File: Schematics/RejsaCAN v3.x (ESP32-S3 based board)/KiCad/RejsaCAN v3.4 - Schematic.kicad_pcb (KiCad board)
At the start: 2 copper layers, 65 parts, among them Q1 SS8050, U1 ESP32-S3-WROOM-1(N16R8), U2 SN65HVD230DR, U3 ME2807A33M3G, U4 LMR14006XDDCR, U5 MT9700

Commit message: Add v3.4 board outline and mounting holes, traced from the fabricated Gerbers
The KiCad board had no Edge.Cuts geometry at all, which blocks placement,
routing and any real fab quote (board price is a function of dimensions).

Both the outline and the holes are derived from upstream manufacturing data
rather than drawn by eye:

  Gerber_BoardOutlineLayer.GKO  -> 8-corner Edge.Cuts profile
  Drill_NPTH_Through.DRL, T03   -> four 2.59mm NPTH mounting holes

Result is 31.496 x 49.530 mm with the 18.034 x 5.969 mm notch between the
top tabs. Verified by exporting Edge.Cuts back out through kicad-cli and
re-measuring: dimensions match the source Gerber, and the notch sits 6.731mm
from both side edges.

Two deliberate choices:

- EasyEDA exported the notch's left wall 0.0007in off vertical. Snapped to
  the mirrored value so both walls are truly vertical; 18um, below any fab
  tolerance, but it makes the outline exactly symmetric as intended.
- The holes are 2.59mm, matching the fabricated board. Stock KiCad offers
  2.5mm (tight for M2.5) and 2.7mm (loose), so RejsaCAN.pretty gains
  MountingHole_2.59mm_NPTH. They carry the board_only attribute, so Update
  PCB from Schematic will not delete them for having no symbol -- confirmed
  by DRC reporting zero schematic-parity errors.

Also gitignores generated fabrication output while keeping a README that
documents how to regenerate it.

Co-Authored-By: Claude Opus 5 (1M context) <noreply@anthropic.com>
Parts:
- added H1: MountingHole_2.59mm_NPTH, RejsaCAN:MountingHole_2.59mm_NPTH, F.Cu at (112.0, 182.5)
- added H2: MountingHole_2.59mm_NPTH, RejsaCAN:MountingHole_2.59mm_NPTH, F.Cu at (139.5, 182.5)
- added H3: MountingHole_2.59mm_NPTH, RejsaCAN:MountingHole_2.59mm_NPTH, F.Cu at (112.0, 227.0)
- added H4: MountingHole_2.59mm_NPTH, RejsaCAN:MountingHole_2.59mm_NPTH, F.Cu at (139.5, 227.0)
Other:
- board outline added: 31.5 x 49.5 mm

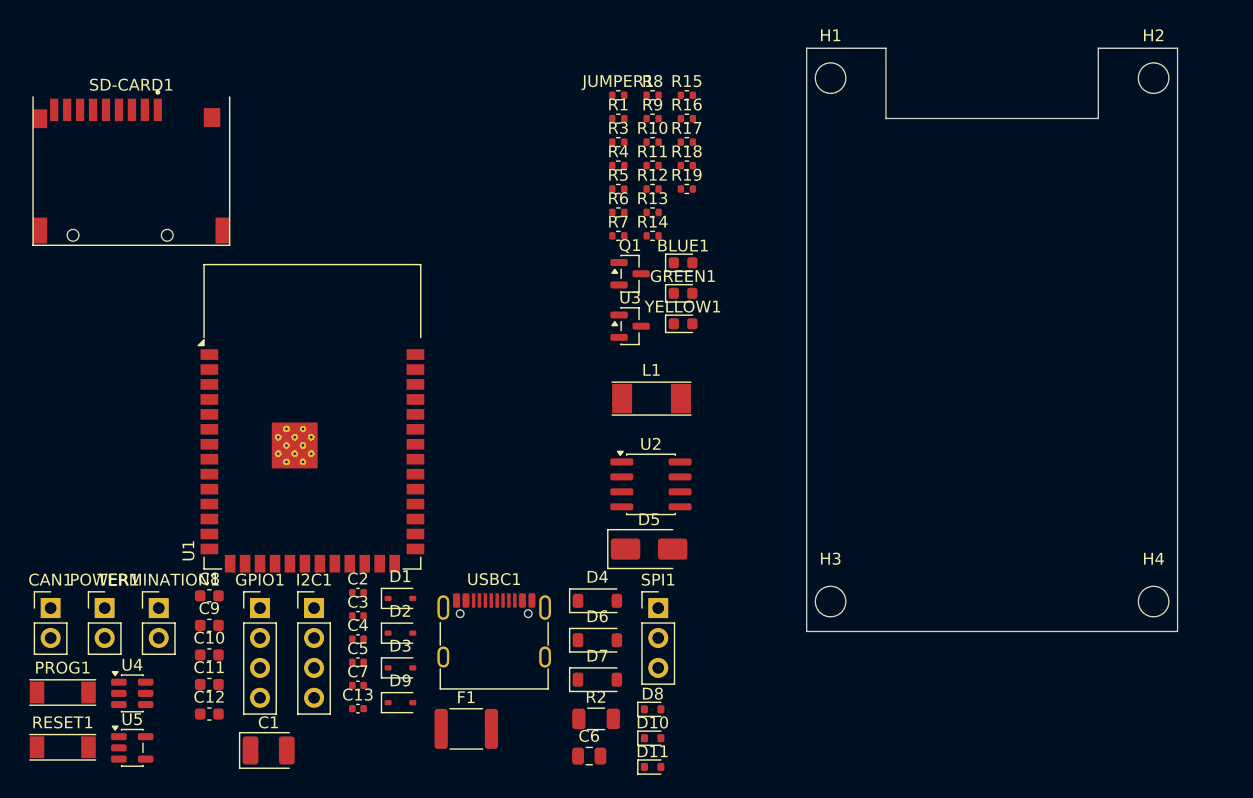
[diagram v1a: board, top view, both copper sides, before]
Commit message: Recover the original v3.4 component placement, and set JLCPCB/automotive rules
Placement is reconstructed from the fabricated board's own manufacturing data
rather than laid out afresh, because the mechanical constraints are fixed: the
connectors must meet the board edges and the 3D-printed cases in this repo are
cut for the original positions.

Method, in decreasing order of certainty:

  1. The solder-mask layers give the complete pad cloud (paste is no good --
     the original skips it for hand-soldered parts). Distinctive multi-pad
     footprints are matched to it by hypothesising rotation and translation,
     most-pads-first so a TSOT-23-6 cannot settle onto 6 of a SOIC-8's pads.
  2. USBC1, U2 and F1 are pinned to hand-identified pad groups; their real land
     patterns differ from the assigned KiCad footprints (see below).
  3. The 2-pad passives are geometrically interchangeable, so which resistor
     lands in which slot is decided electrically -- a maximum-matching pass for
     feasibility, then descent on total half-perimeter wirelength. Every such
     assignment is electrically valid since the netlist is fixed; only
     routability differs, and the original was hand-optimised, so minimum
     wirelength reproduces it where it was in fact optimal.

Result: 216 of 232 original pads are covered, 65/65 footprints sit on the
board, SD-CARD1 and JUMPER1 correctly move to the bottom side, and DRC reports
zero schematic-parity errors and zero shorts. The 16 uncovered pads are
through-holes and a 2-pad land the schematic has no part for -- this board was
fabricated with more pads than the v3.4 schematic accounts for.

R16 is the one part not recovered: the fabricated board is one 0402 land short
of the 25 this schematic needs, so R16 is parked in clear space and flagged
rather than forced onto a land that is not its own.

Three footprints do not match what was actually built, which is worth knowing
before ordering:
  - USB-C   shell legs sit 0.467mm from w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
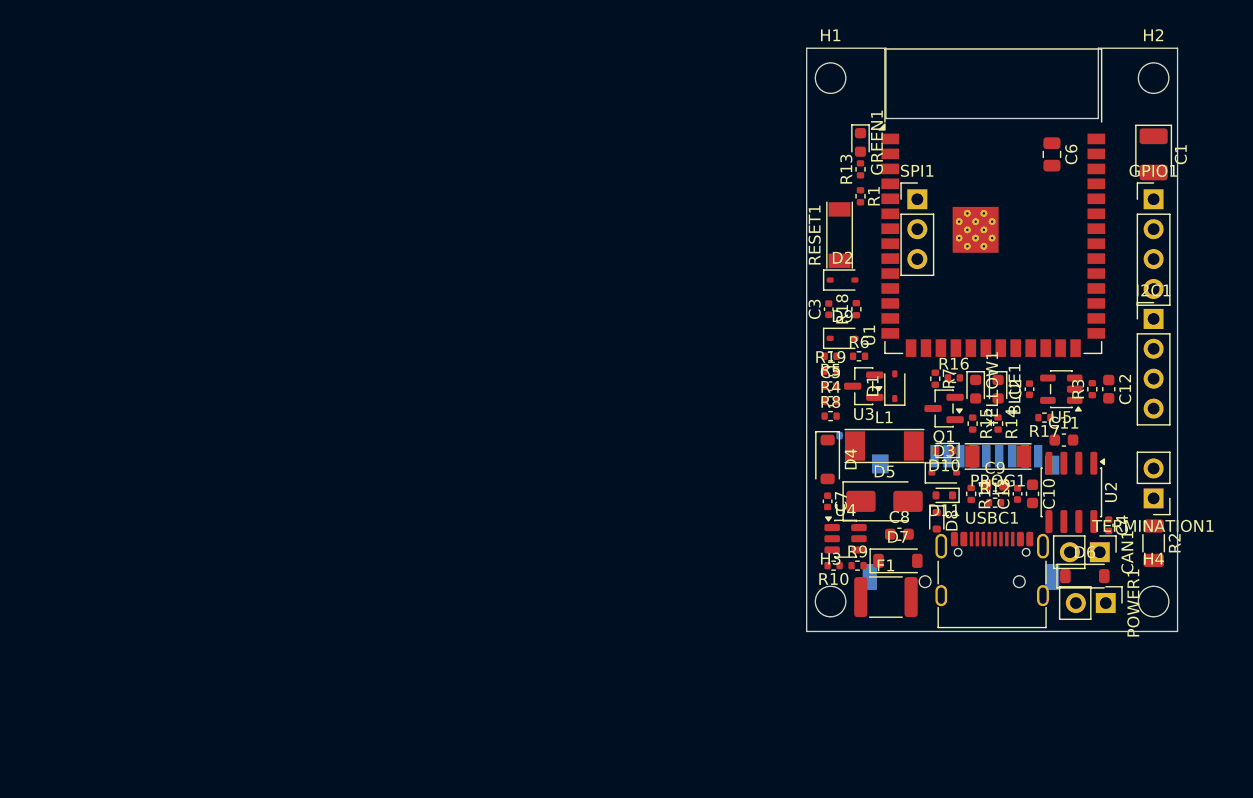
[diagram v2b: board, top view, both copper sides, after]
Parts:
- JUMPER1, SD-CARD1: moved to B.Cu
- moved C1 90.6 mm to (139.5, 189.0), turned to -90 degrees
- moved CAN1 89.2 mm to (134.9, 222.8), turned to -90 degrees
- moved POWER1 85.0 mm to (135.4, 227.1), turned to -90 degrees
- moved TERMINATION1 85.0 mm to (139.5, 218.2), turned to 180 degrees
- moved U5 84.6 mm to (131.6, 209.0), turned to 180 degrees
- moved GPIO1 83.5 mm to (139.5, 192.8)
- moved PROG1 81.9 mm to (126.3, 214.7), turned to 180 degrees
- moved C12 81.2 mm to (135.7, 209.0), turned to -90 degrees
- moved RESET1 79.0 mm to (112.8, 195.9), turned to 90 degrees
- moved SD-CARD1 76.4 mm to (123.1, 219.8), turned to 180 degrees
- moved C11 75.5 mm to (131.8, 213.3)
- moved I2C1 75.4 mm to (139.5, 203.0)
- moved C10 71.2 mm to (129.2, 217.8), turned to -90 degrees
- moved C9 67.8 mm to (126.0, 217.1)
- moved C4 64.5 mm to (135.7, 220.5), turned to -90 degrees
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
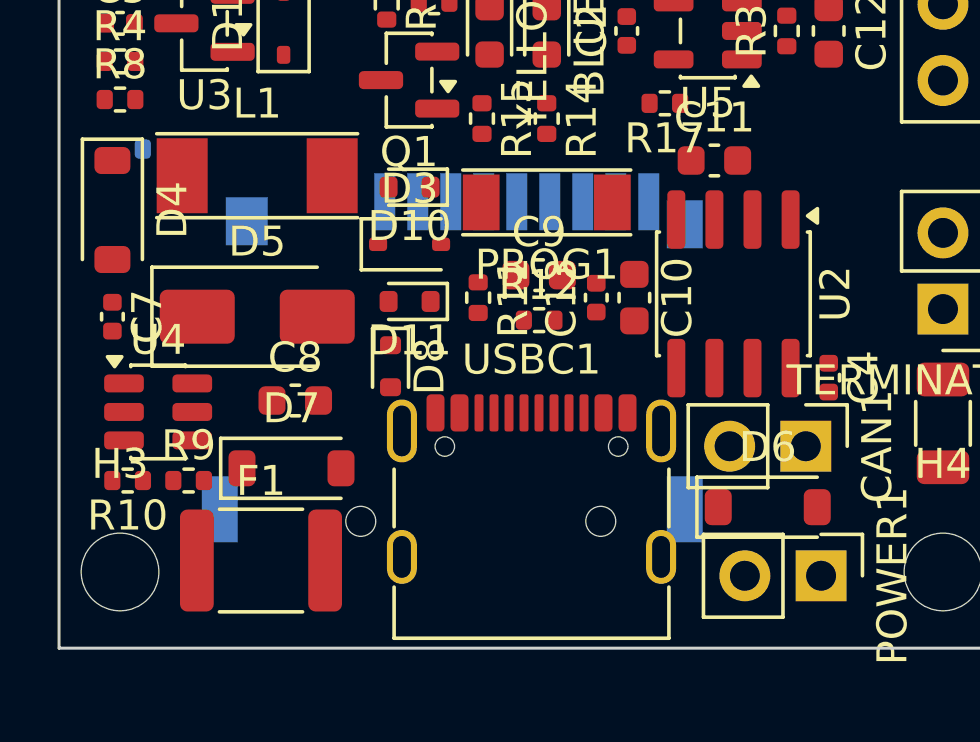
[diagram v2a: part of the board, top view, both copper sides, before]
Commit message: Correct three footprints to the land patterns actually fabricated
Measured from the v3.4 manufacturing data -- top-copper flashes for the pads,
the NPTH drill file for the board locks -- rather than trusted from the stock
libraries:

  F1     pad pitch 3.706mm and 1.407 x 3.500 pads; KiCad's 1812 land is 4.276mm
  U2     SOIC-8 rows 5.544mm apart with 2.045 x 0.588 pads, not 4.95 / 1.95x0.60
  USBC1  shell legs 1.067 and 5.267mm below the contact row (library said 0.600
         and 4.800); NPTH board locks 1.676mm below it (library said 1.120)

All three now sit on their original pads to 0-1 um, and board pad coverage rises
from 216 to 225 of 232. F1 and U2 move to project-local footprints so the fix
cannot be silently undone by a library update; the schematic's footprint fields
move with them, verified by re-exporting the BOM.

This clears every electrical DRC violation. The two that remained were caused by
the wrong geometry: with U2's real 2.045mm pads it comes within 0.189mm of C11,
which is the board that was actually built and is inside JLCPCB's 0.15mm SMD
pad-to-pad floor. A third custom rule allows that spacing between pads while
keeping the full net-class clearance for tracks and vias -- component choice
sets pad spacing, the router should not be let off the same hook.

Remaining DRC is non-electrical: silkscreen text overlaps, courtyard overlaps
(KiCad's courtyards are more generous than EasyEDA's), and the top two mounting
holes falling in the stock module footprint's antenna keepout.

Co-Authored-By: Claude Opus 5 (1M context) <noreply@anthropic.com>
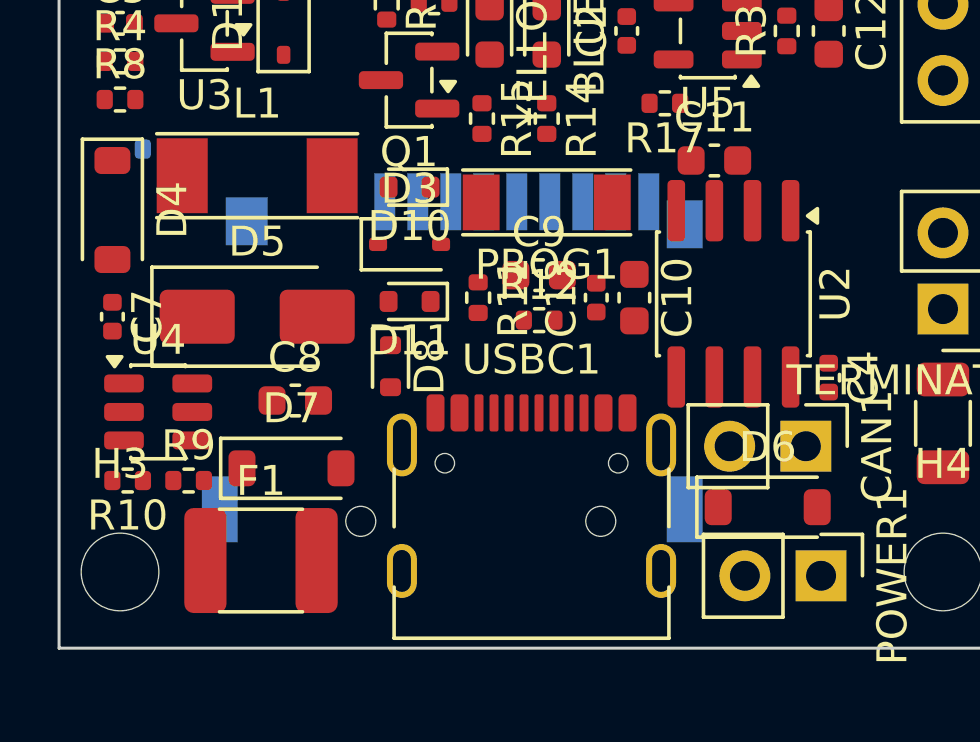
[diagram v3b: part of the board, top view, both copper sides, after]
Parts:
- F1: footprint Fuse:Fuse_1812_4532Metric -> RejsaCAN:Fuse_1812_RejsaCAN_3.706mm
- U2: footprint Package_SO:SOIC-8_3.9x4.9mm_P1.27mm -> RejsaCAN:SOIC-8_RejsaCAN_5.544mm
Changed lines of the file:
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@@
 		)
 		(pad "" np_thru_hole circle
-			(at -2.89 -2.605)
+			(at -2.89 -2.049)
 			(size 0.65 0.65)
 			(drill 0.65)
@@
 		)
 		(pad "" np_thru_hole circle
-			(at 2.89 -2.605)
+			(at 2.89 -2.049)
 			(size 0.65 0.65)
 			(drill 0.65)
@@
 		)
 		(pad "1" thru_hole oval
-			(at -4.32 -3.125)
+			(at -4.32 -2.658)
 			(size 1 2.1)
 			(drill oval 0.6 1.7)
@@
 		)
 		(pad "2" thru_hole oval
-			(at -4.32 1.075)
+			(at -4.32 1.542)
 			(size 1 1.8)
 			(drill oval 0.6 1.4)
@@
 		)
 		(pad "3" thru_hole oval
-			(at 4.32 -3.125)
+			(at 4.32 -2.658)
 			(size 1 2.1)
 			(drill oval 0.6 1.7)
@@
 		)
 		(pad "4" thru_hole oval
-			(at 4.32 1.075)
+			(at 4.32 1.542)
 			(size 1 1.8)
 			(drill oval 0.6 1.4)
@@
 		)
 	)
-	(footprint "Package_SO:SOIC-8_3.9x4.9mm_P1.27mm"
+	(footprint "RejsaCAN:SOIC-8_RejsaCAN_5.544mm"
 		(layer "F.Cu")
 		(at 132.479 217.718999 -90)
@@
 		)
 		(pad "1" smd roundrect
-			(at -2.475 -1.905 270)
-			(size 1.95 0.6)
+			(at -2.772 -1.905 270)
+			(size 2.045 0.588)
 			(layers "F.Cu" "F.Mask" "F.Paste")
 			(roundrect_rratio 0.25)
@@
 		)
 		(pad "2" smd roundrect
-			(at -2.475 -0.635 270)
-			(size 1.95 0.6)
+			(at -2.772 -0.635 270)
+			(size 2.045 0.588)
 			(layers "F.Cu" "F.Mask" "F.Paste")
 			(roundrect_rratio 0.25)
@@
 		)
 		(pad "3" smd roundrect
-			(at -2.475 0.635 270)
-			(size 1.95 0.6)
+			(at -2.772 0.635 270)
+			(size 2.045 0.588)
 			(layers "F.Cu" "F.Mask" "F.Paste")
 			(roundrect_rratio 0.25)
@@
 		)
 		(pad "4" smd roundrect
-			(at -2.475 1.905 270)
-			(size 1.95 0.6)
+			(at -2.772 1.905 270)
+			(size 2.045 0.588)
 			(layers "F.Cu" "F.Mask" "F.Paste")
 			(roundrect_rratio 0.25)
@@
 		)
 		(pad "5" smd roundrect
-			(at 2.475 1.905 270)
-			(size 1.95 0.6)
+			(at 2.772 1.905 270)
+			(size 2.045 0.588)
 			(layers "F.Cu" "F.Mask" "F.Paste")
 			(roundrect_rratio 0.25)
@@
 		)
 		(pad "6" smd roundrect
-			(at 2.475 0.635 270)
-			(size 1.95 0.6)
+			(at 2.772 0.635 270)
+			(size 2.045 0.588)
 			(layers "F.Cu" "F.Mask" "F.Paste")
 			(roundrect_rratio 0.25)
@@
 		)
 		(pad "7" smd roundrect
-			(at 2.475 -0.635 270)
-			(size 1.95 0.6)
+			(at 2.772 -0.635 270)
+			(size 2.045 0.588)
 			(layers "F.Cu" "F.Mask" "F.Paste")
 			(roundrect_rratio 0.25)
@@
 		)
 		(pad "8" smd roundrect
-			(at 2.475 -1.905 270)
-			(size 1.95 0.6)
+			(at 2.772 -1.905 270)
+			(size 2.045 0.588)
 			(layers "F.Cu" "F.Mask" "F.Paste")
 			(roundrect_rratio 0.25)
@@
 		)
 	)
-	(footprint "Fuse:Fuse_1812_4532Metric"
+	(footprint "RejsaCAN:Fuse_1812_RejsaCAN_3.706mm"
 		(layer "F.Cu")
 		(at 116.731 226.609)
@@
 		)
 		(pad "1" smd roundrect
-			(at -2.1375 0)
-			(size 1.125 3.4)
+			(at -1.853 0)
+			(size 1.407 3.5)
 			(layers "F.Cu" "F.Mask" "F.Paste")
 			(roundrect_rratio 0.222222)
@@
 		)
 		(pad "2" smd roundrect
-			(at 2.1375 0)
-			(size 1.125 3.4)
+			(at 1.853 0)
+			(size 1.407 3.5)
 			(layers "F.Cu" "F.Mask" "F.Paste")
 			(roundrect_rratio 0.222222)
